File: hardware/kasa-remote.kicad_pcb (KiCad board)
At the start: 2 copper layers, 40 parts, among them J1 USB4105-GF-A, J2 S2B-PH-SM4-TB, J3 sh1106_vert, J4 sh1106_horiz, Q1 DMP2045U-7, SW1 RotaryEncoder_Switch, SW10 SW_Push, SW11 SW_Push, SW12 BOOT0, SW2 SW_Push, SW3 SW_Push, SW4 SW_Push, SW5 SW_Push, SW6 SW_Push, SW7 SW_Push, SW8 SW_Push, SW9 SW_Push, U1 ESP32-S3-WROOM-1-N4, U2 MAX17048G+T10, U4 MCP73831T-2ACI/OT, U5 AP2112K-3.3

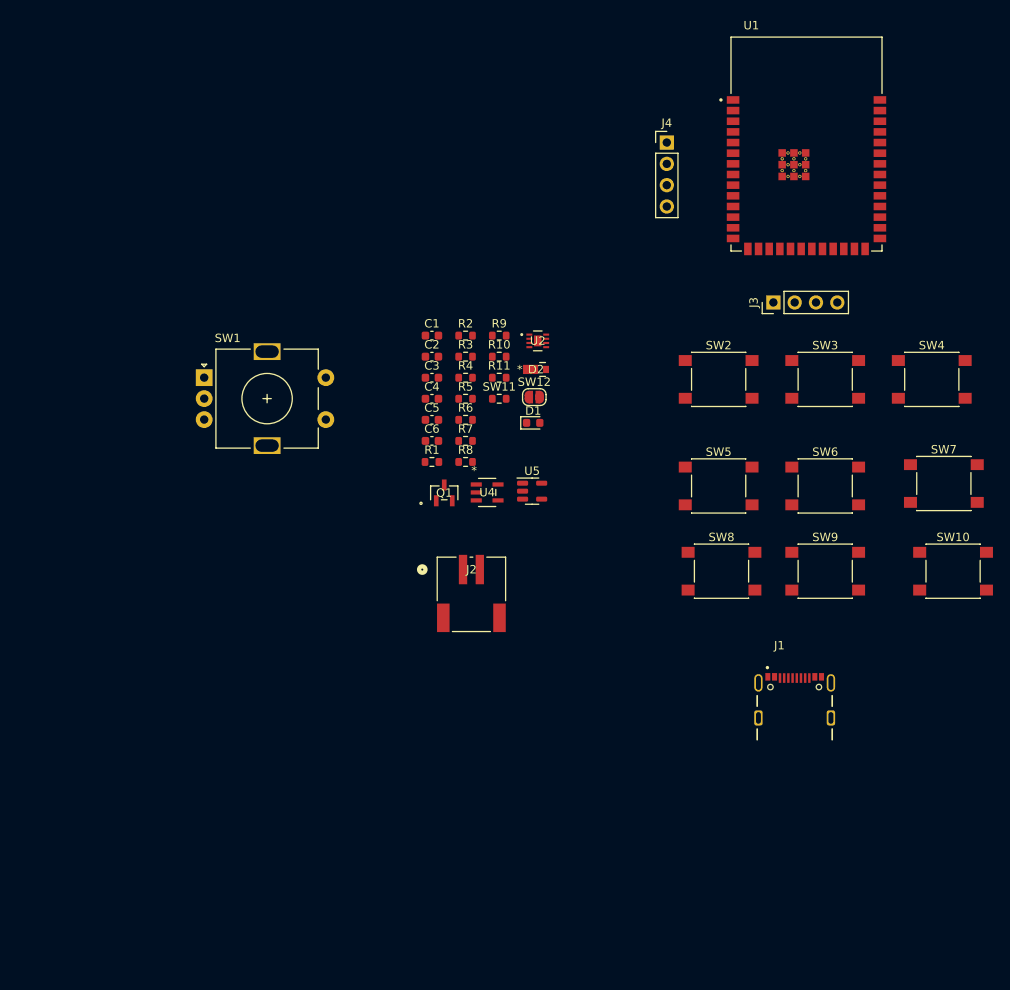
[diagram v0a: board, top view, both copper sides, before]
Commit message: fixed a couple mistakes in the schematic, organizing and starting layout
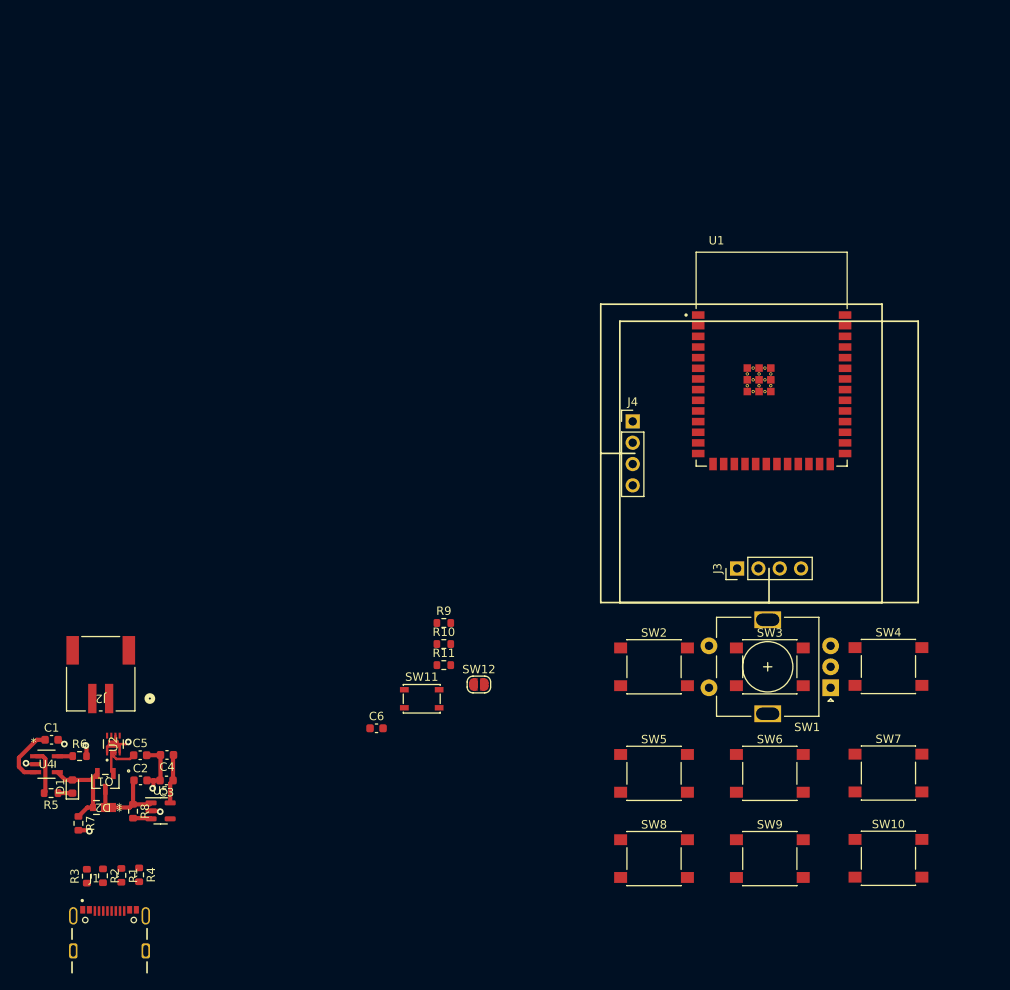
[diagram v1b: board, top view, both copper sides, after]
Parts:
- SW11: footprint Resistor_SMD:R_0603_1608Metric -> Button_Switch_SMD:SW_SPST_PTS810
- moved J1 86.3 mm to (103.8, 139.5)
- moved SW1 83.3 mm to (189.7, 108.2), turned to 180 degrees
- moved R2 77.5 mm to (103.0, 130.6), turned to -90 degrees
- moved R3 76.6 mm to (101.1, 130.6), turned to 90 degrees
- moved D2 73.4 mm to (103.0, 122.4), turned to 180 degrees
- moved R4 70.9 mm to (107.3, 130.5), turned to -90 degrees
- moved D1 70.0 mm to (99.3, 119.9), turned to 90 degrees
- moved U2 69.8 mm to (104.2, 114.9), turned to 90 degrees
- moved R5 68.2 mm to (96.8, 120.7), turned to 180 degrees
- moved C1 66.2 mm to (96.9, 114.4)
- moved R7 64.9 mm to (100.1, 124.3), turned to -90 degrees
- moved U4 61.7 mm to (96.2, 117.3)
- moved R1 61.6 mm to (105.2, 130.5), turned to -90 degrees
- moved C2 61.3 mm to (107.5, 119.2)
- moved R6 61.0 mm to (100.2, 116.3)
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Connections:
- R6 pad 1: unconnected-(R6-Pad1) -> Net-(U4-PROG)
- U4 pad 5: unconnected-(U4-PROG-Pad5) -> Net-(U4-PROG)
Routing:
- net GND: track 0.00 -> 19.4 mm, vias 0 -> 7
- net +BATT: track 0.00 -> 13.9 mm
- net VBUS: track 0.00 -> 11.2 mm
- net Net-(D2-K): track 0.00 -> 10.5 mm
- net +3.3V: track 0.00 -> 5.87 mm
- net Net-(U4-STAT): track 0.00 -> 5.44 mm
- net Net-(U5-EN): track 0.00 -> 2.18 mm
- net Net-(U4-PROG): track 0.00 -> 1.83 mm
- net Net-(D1-K): track 0.00 -> 1.72 mm

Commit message: layout just about done, no more errors at least
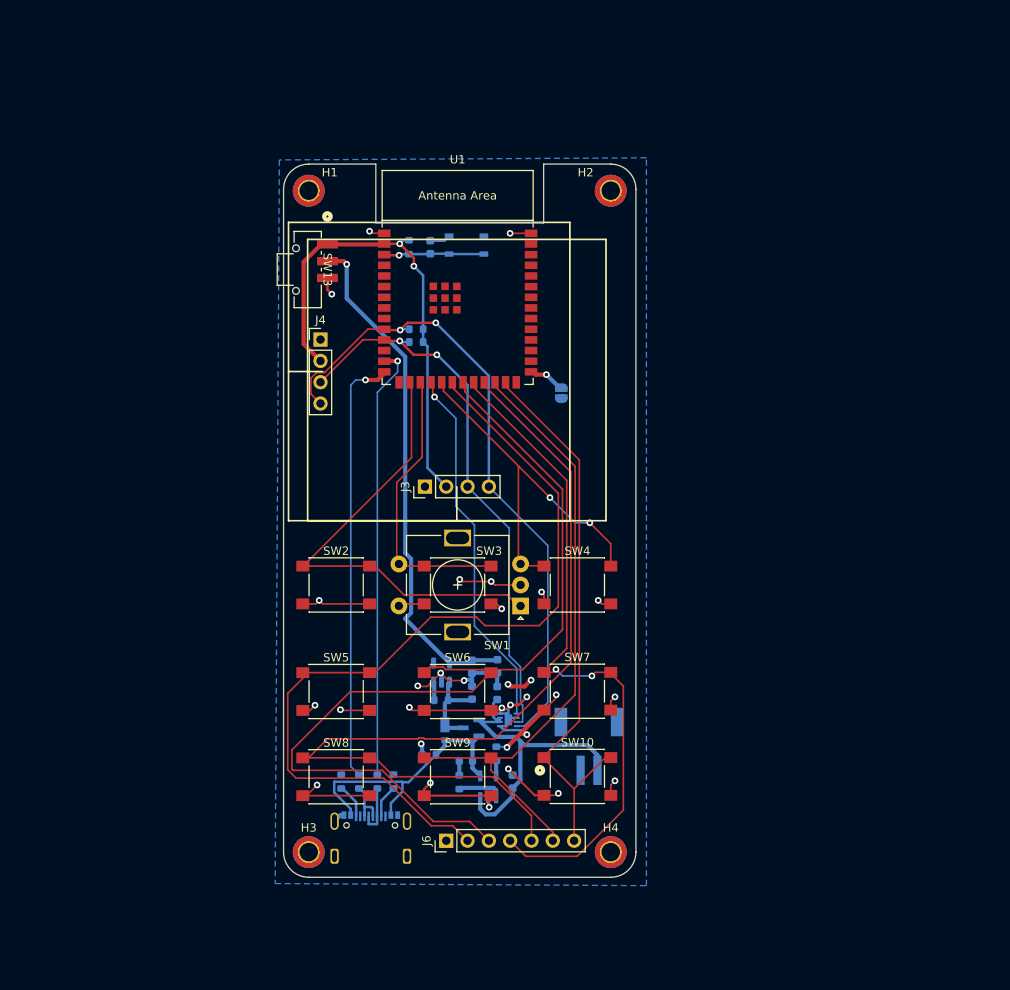
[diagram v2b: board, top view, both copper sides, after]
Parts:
- added H1: MountingHole_Pad, MountingHole:MountingHole_2.2mm_M2_DIN965_Pad_TopBottom, F.Cu at (127.5, 48.9)
- added H2: MountingHole_Pad, MountingHole:MountingHole_2.2mm_M2_DIN965_Pad_TopBottom, F.Cu at (163.5, 48.9)
- added H3: MountingHole_Pad, MountingHole:MountingHole_2.2mm_M2_DIN965_Pad_TopBottom, F.Cu at (127.5, 127.8)
- added H4: MountingHole_Pad, MountingHole:MountingHole_2.2mm_M2_DIN965_Pad_TopBottom, F.Cu at (163.5, 127.8)
- added J6: Button_breakout, Connector_PinHeader_2.54mm:PinHeader_1x07_P2.54mm_Vertical, F.Cu at (143.9, 126.4)
- added SW13: CSS-1210TB, CSS-1210TB:CSS-1210TB_NDC, F.Cu at (127.4, 58.3)
- C1, C2, C3, C4, C5, C6, D1, D2, J1, J2, Q1, R1, R10, R11, R2, R3, R4, R5, R6, R7, R8, R9, SW11, SW12, U2, U4, U5: moved to B.Cu
- U1: footprint ESP32-S3-WROOM-1-N4:XCVR_ESP32-S3-WROOM-1-N4 -> PCM_Espressif:ESP32-S3-WROOM-1
- moved J2 58.8 mm to (160.9, 115.0), turned to 0 degrees
- moved C6 57.7 mm to (142.0, 55.7), turned to 90 degrees
- moved C1 55.2 mm to (151.8, 119.4), turned to 90 degrees
- moved SW11 54.3 mm to (146.3, 55.4)
- moved U4 52.7 mm to (148.9, 120.0), turned to 90 degrees
- moved R11 50.0 mm to (139.4, 55.7), turned to 90 degrees
- moved R6 49.7 mm to (149.9, 116.0), turned to 90 degrees
- moved R5 48.7 mm to (145.5, 119.4), turned to -90 degrees
- moved U2 47.2 mm to (151.3, 112.0), turned to 0 degrees
- moved D1 47.0 mm to (146.2, 116.9), turned to 0 degrees
- moved Q1 44.0 mm to (146.8, 112.9), turned to -90 degrees
- moved C5 43.2 mm to (150.0, 108.8), turned to 90 degrees
- moved R7 42.6 mm to (141.8, 116.2), turned to 180 degrees
- moved D2 41.8 mm to (143.7, 113.2), turned to -90 degrees
- moved C2 40.9 mm to (147.0, 108.8), turned to 90 degrees
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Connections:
- C3 pad 1: +3.3V -> 3.3v_sw
- C4 pad 1: +3.3V -> 3.3v_sw
- U5 pad 5: +3.3V -> 3.3v_sw
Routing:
- net btn5: track 0.00 -> 110.0 mm
- net GND: track 19.4 -> 127.6 mm, vias 7 -> 29
- net btn7: track 0.00 -> 106.1 mm
- net btn4: track 0.00 -> 103.3 mm
- net btn6: track 0.00 -> 82.5 mm, vias 0 -> 2
- net SDA: track 0.00 -> 78.0 mm, vias 0 -> 2
- net btn8: track 0.00 -> 75.1 mm
- net btn9: track 0.00 -> 67.5 mm
- net SCL: track 0.00 -> 66.6 mm, vias 0 -> 2
- net 3.3v_sw: track 0.00 -> 61.5 mm, vias 0 -> 1
- net btn1: track 0.00 -> 54.0 mm
- net D+: track 0.00 -> 51.7 mm, vias 0 -> 1
- net D-: track 0.00 -> 51.7 mm, vias 0 -> 1
- net +3.3V: track 5.87 -> 57.5 mm, vias 0 -> 2
- net btn3: track 0.00 -> 46.3 mm, vias 0 -> 2
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- added copper zone on B.Cu, net GND
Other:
- board outline added: 42 x 85 mm

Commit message: still tweaking silkscreens
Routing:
- net (no net): track 3.16 -> 0.00 mm, vias 2 -> 0
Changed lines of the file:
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@@
     (property "ki_keywords" "R resistor")
     (attr smd)
-    (fp_text reference "R8" (at 0 1.43) (layer "B.SilkS")
+    (fp_text reference "R8" (at 2.2826 0.1434) (layer "B.SilkS")
         (effects (font (size 1 1) (thickness 0.15)) (justify mirror))
     )
@@
     (property "ki_keywords" "capacitor cap")
     (attr smd)
-    (fp_text reference "C3" (at 0 1.43 90) (layer "B.SilkS")
+    (fp_text reference "C3" (at -2.1534 -0.0474 90) (layer "B.SilkS")
         (effects (font (size 1 1) (thickness 0.15)) (justify mirror))
     )
@@
     (property "ki_keywords" "linear regulator ldo fixed positive")
     (attr smd)
-    (fp_text reference "U5" (at 0 2.4 90) (layer "B.SilkS")
+    (fp_text reference "U5" (at 2.3559 -0.0826 90) (layer "B.SilkS")
         (effects (font (size 1 1) (thickness 0.15)) (justify mirror))
     )
@@
   (gr_line (start 155.5 45.75) (end 163.5 45.75)
     (stroke (width 0.1) (type default)) (layer "Edge.Cuts"))
-  (segment (start 153.25 108) (end 154 107.25) (width 0.5) (layer "F.Cu") (net 0))
-  (segment (start 151.5 108) (end 153.25 108) (width 0.5) (layer "F.Cu") (net 0))
-  (segment (start 151.5 108) (end 151.25 107.75) (width 0.5) (layer "F.Cu") (net 0))
-  (via (at 154 107.25) (size 0.8) (drill 0.4) (layers "F.Cu" "B.Cu") (net 0))
-  (via (at 151.25 107.75) (size 0.8) (drill 0.4) (layers "F.Cu" "B.Cu") (net 0))
   (segment (start 147.7824 111.9909) (end 149.8157 114.0242) (width 0.5) (layer "B.Cu") (net 1))
   (segment (start 149.5146 111.645299) (end 149.5146 110.0164) (width 0.3) (layer "B.Cu") (net 1))

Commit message: cleaned up the silkscreen errors
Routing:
- net GND: track 127.6 -> 126.3 mm, vias 29 -> 28
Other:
- outline, holes or cut-outs redrawn

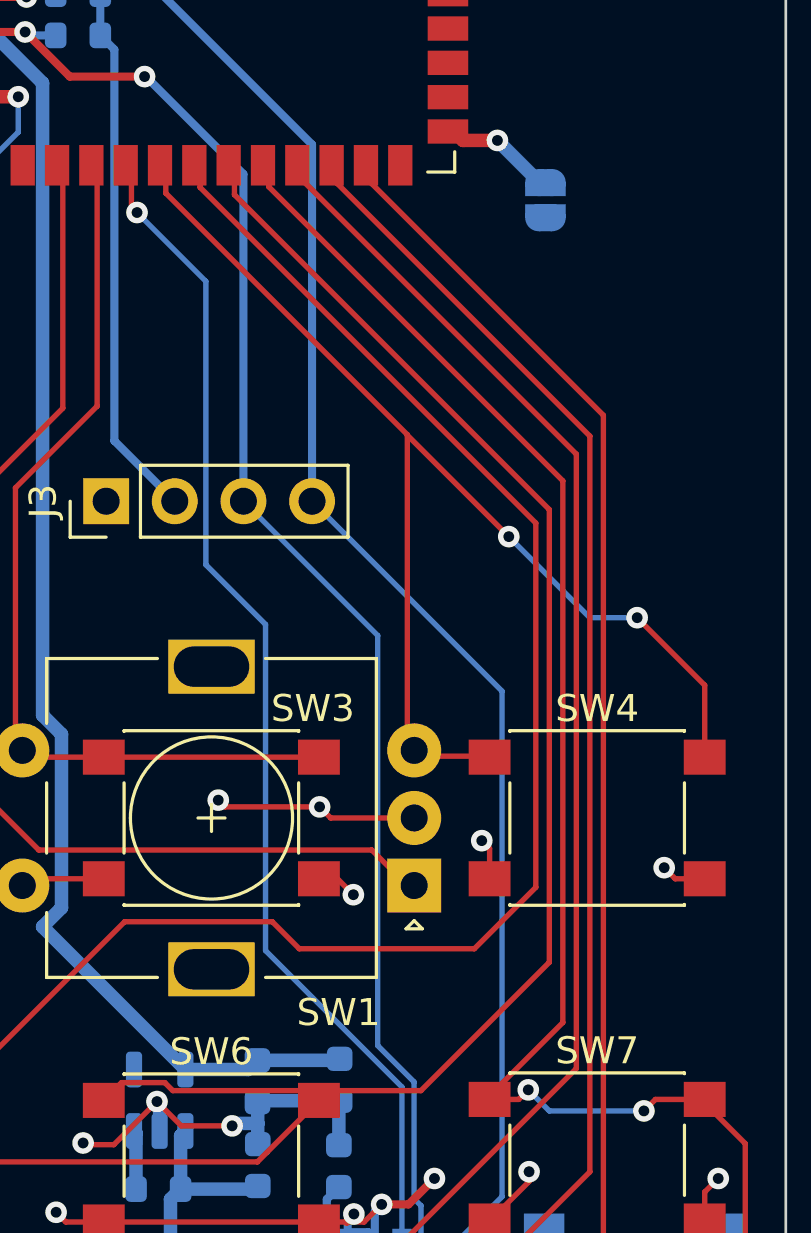
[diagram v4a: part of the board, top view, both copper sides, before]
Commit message: just about done, I think I want to move the horizontal display over a bit so it's symetrical to the pcb
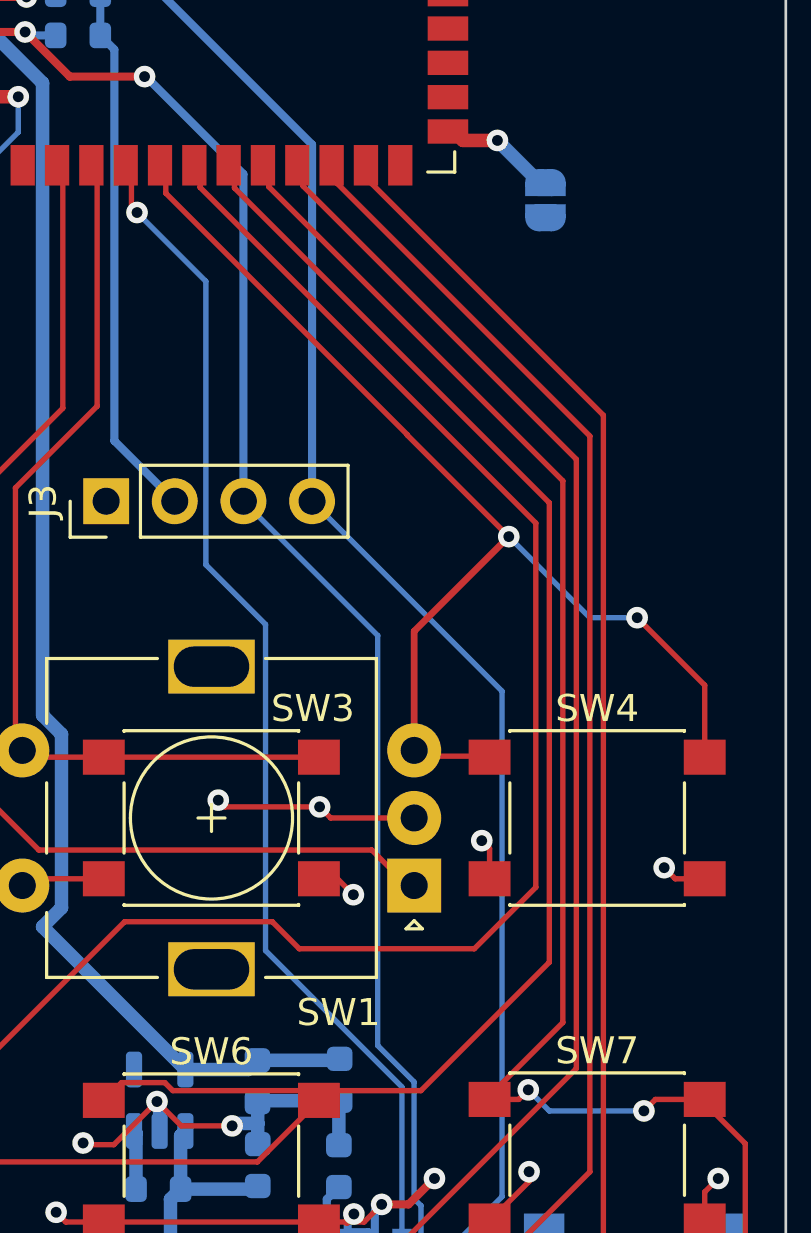
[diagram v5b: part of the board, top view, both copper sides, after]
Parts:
- added G***: LOGO, duck:cigcat_small, B.Cu at (160.0, 58.5)
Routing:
- net btn3: track 46.3 -> 43.9 mm
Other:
- board text added: "Matthew Smith 2024"

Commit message: added the waywayway for pcb way, also added the bom spreadsheet
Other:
- board text added: "WayWayWay"
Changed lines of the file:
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@@
     (effects (font (size 1 1) (thickness 0.125)) (justify left bottom mirror))
+  )
+  (gr_text "WayWayWay" (at 156 66) (layer "B.SilkS")
+    (effects (font (size 1 1) (thickness 0.2) bold) (justify left bottom mirror))
   )
   (segment (start 147.7824 111.9909) (end 149.8157 114.0242) (width 0.5) (layer "B.Cu") (net 1))
